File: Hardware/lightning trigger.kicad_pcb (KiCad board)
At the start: 2 copper layers, 40.5 x 70 mm, 59 parts, among them J1 Conn_01x02, J2 Conn_02x03_Odd_Even, J3 Conn_01x04, J4 PJ-237-6A, J5 PJ-237-6A, J6 USB_OTG, J7 Conn_01x01, J8 Conn_01x01, Q1 Q_Photo_NPN, Q2 2N3904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

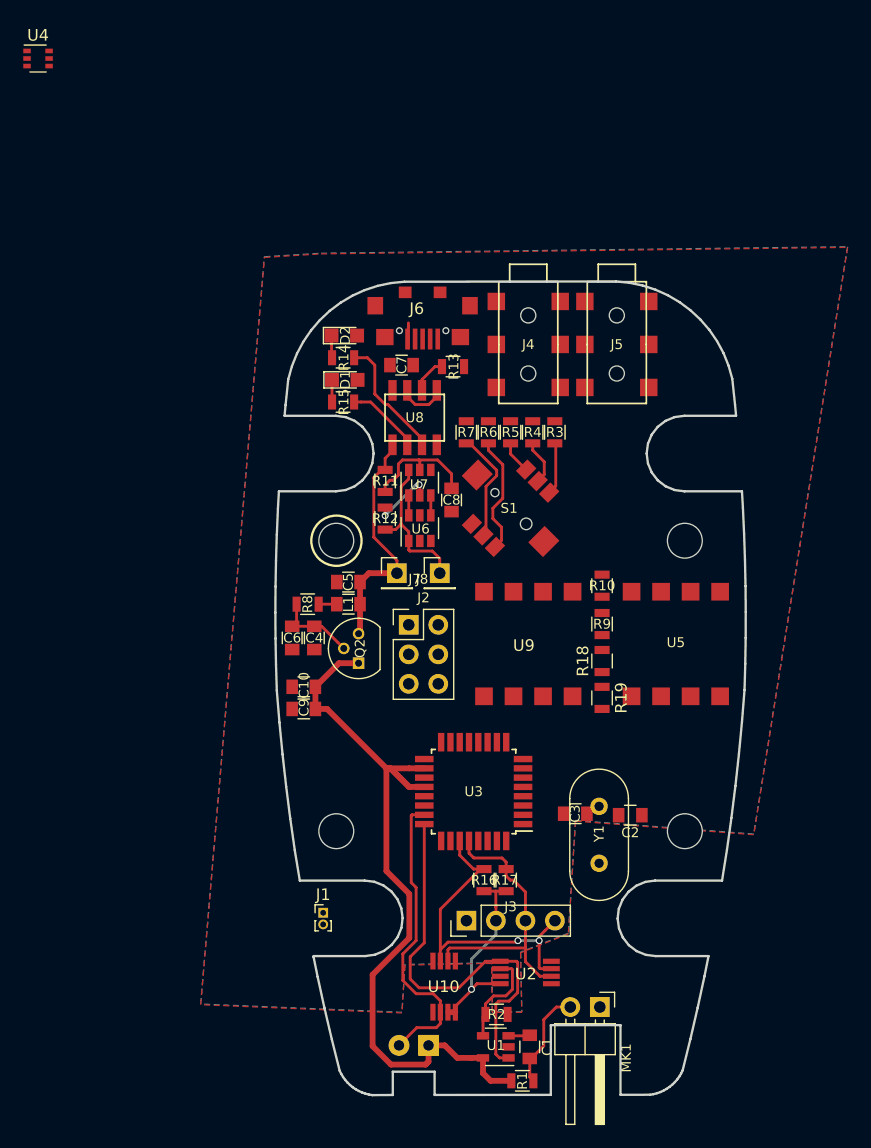
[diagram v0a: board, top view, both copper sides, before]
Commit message: re-drew board outline to make it larger
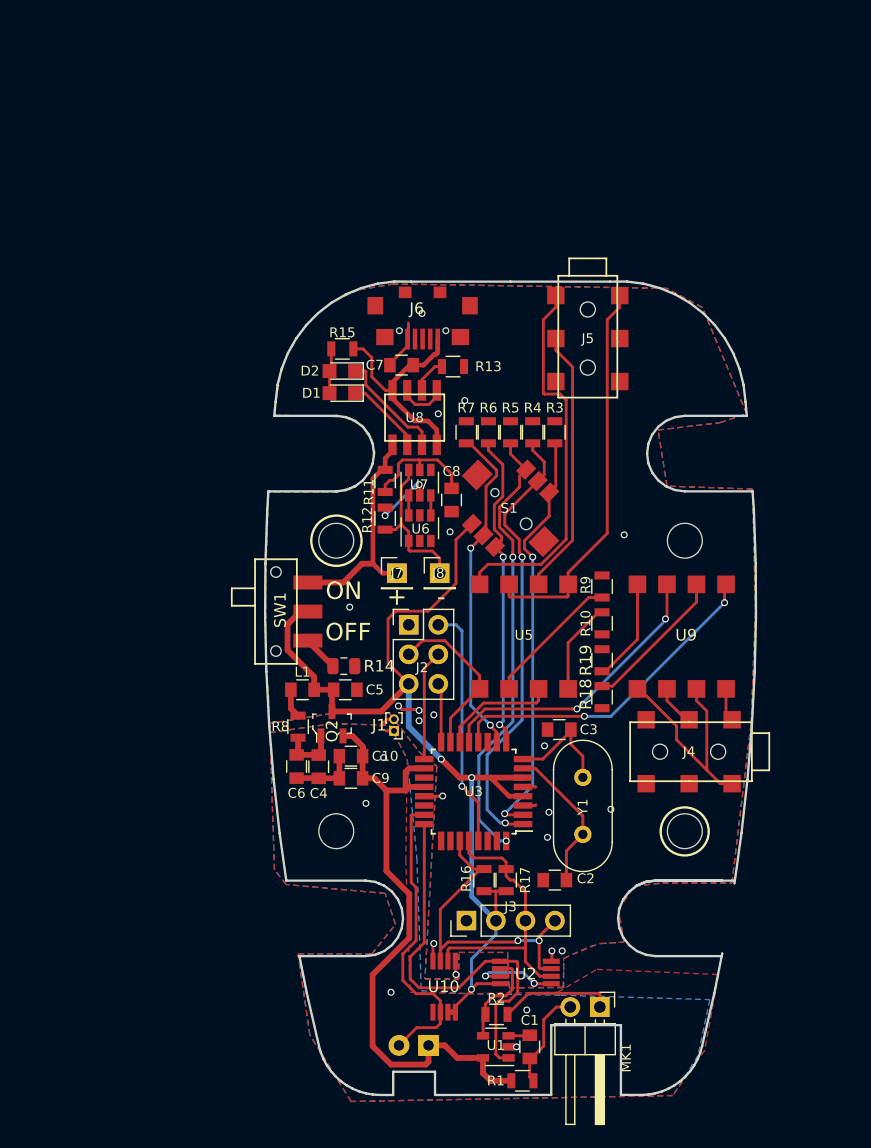
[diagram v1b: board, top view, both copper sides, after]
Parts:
- removed U4: TPL0401A, Package_TO_SOT_SMD:SOT-363_SC-70-6
- added SW1: SW_SPDT, Switches:JS102011SAQN, F.Cu at (-20.2, -6.60)
- Q2: value 2N3904 -> BC846B_215; footprint TO_SOT_Packages_THT:TO-92_Molded_Narrow -> digikey-footprints:SOT-23-3
- R14: footprint Resistors_SMD:R_0805 -> Resistor_SMD:R_0805_2012Metric
- R15: value 1.1k -> 1k
- moved J4 37.7 mm to (15.4, 5.46), turned to 270 degrees
- moved R14 26.5 mm to (-14.4, -1.91)
- moved J1 16.8 mm to (-10.0, 3.67), turned to 180 degrees
- moved U9 13.2 mm to (14.7, -4.45), turned to 270 degrees
- moved U5 13.1 mm to (1.14, -4.45)
- moved C4 11.1 mm to (-16.5, 6.75)
- moved C6 11.1 mm to (-18.4, 6.73)
- moved R8 10.6 mm to (-18.3, 3.30), turned to 90 degrees
- moved C5 9.27 mm to (-14.2, 0.13), turned to 0 degrees
- moved C2 8.57 mm to (3.81, 16.5)
- moved L1 8.36 mm to (-17.9, 0.13)
- moved C3 7.37 mm to (4.19, 3.56)
- moved C10 7.22 mm to (-13.7, 5.84)
- moved C9 7.22 mm to (-13.7, 7.75)
- moved Q2 5.69 mm to (-15.4, 3.05)
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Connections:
- C10 pad 2: GNDA -> GNDD
- C4 pad 2: GNDA -> GNDD
- C5 pad 1: +BATT -> VIN
- C6 pad 2: GNDA -> GNDD
- C9 pad 2: GNDA -> GNDD
- D1 pad 2: Net-(C7-Pad1) -> Net-(D1-Pad2)
- D2 pad 2: Net-(C7-Pad1) -> Net-(D1-Pad2)
- J1 pad 1: GNDA -> GNDD
- J2 pad 5: +BATT -> VIN
- J3 pad 2: +BATT -> VIN
- L1 pad 2: +BATT -> VIN
- MK1 pad 1: GNDA -> GNDD
- Q2 pad 1: VDDA -> Net-(C4-Pad1)
- Q2 pad 2: Net-(C4-Pad1) -> VDDA
- Q2 pad 3: +BATT -> VIN
- R14 pad 1: Net-(D2-Pad1) -> Net-(R14-Pad1)
- R14 pad 2: Net-(R14-Pad2) -> GNDD
- R15 pad 1: Net-(D1-Pad1) -> Net-(C7-Pad1)
- R15 pad 2: Net-(R15-Pad2) -> Net-(D1-Pad2)
- R16 pad 1: +BATT -> VIN
- R17 pad 1: +BATT -> VIN
- R2 pad 1: GNDA -> GNDD
- S1 pad 6: +BATT -> VIN
- U1 pad 2: GNDA -> GNDD
- U10 pad 5: GNDA -> GNDD
- U10 pad 7: +BATT -> VIN
- U10 pad 8: +BATT -> VIN
- U2 pad 8: +BATT -> VIN
- U3 pad 1: RIGHT -> CENTER
- U3 pad 10: LEFT -> RIGHT
- U3 pad 2: UP -> LEFT
- U3 pad 4: +BATT -> VIN
- U3 pad 6: +BATT -> VIN
- U3 pad 9: CENTER -> UP
- U5 pad 1: FOCUS -> FOCUS2
- U5 pad 3: SHUTTER -> SHUTTER2
- U8 pad 6: Net-(R15-Pad2) -> Net-(D1-Pad1)
- U8 pad 7: Net-(R14-Pad2) -> Net-(D2-Pad1)
- U9 pad 1: FOCUS2 -> SHUTTER
- U9 pad 3: SHUTTER2 -> FOCUS
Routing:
- net VIN: track 0.00 -> 88.1 mm, vias 0 -> 3
- net GNDD: track 6.33 -> 44.2 mm, vias 0 -> 26
- net DOWN: track 2.82 -> 38.7 mm, vias 0 -> 2
- net CENTER: track 3.90 -> 38.8 mm, vias 0 -> 2
- net Net-(J5-Pad1): track 0.00 -> 33.9 mm
- net Net-(J5-Pad4): track 0.00 -> 32.7 mm
- net LEFT: track 4.51 -> 35.9 mm, vias 0 -> 2
- net SHUTTER: track 0.00 -> 28.8 mm, vias 0 -> 2
- net FOCUS: track 0.00 -> 25.3 mm, vias 0 -> 2
- net Net-(J5-Pad2): track 0.00 -> 23.0 mm
- net RST: track 0.00 -> 20.9 mm, vias 0 -> 1
- net Net-(J4-Pad1): track 0.00 -> 19.6 mm
- net Net-(C7-Pad1): track 0.00 -> 19.5 mm
- net RIGHT: track 9.65 -> 28.8 mm, vias 0 -> 2
- net +BATT: track 37.8 -> 19.8 mm, vias 1 -> 0
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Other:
- board size 40.5 x 70 mm -> 42.2 x 70 mm
- board text added: "+"
- board text added: "-"
- board text added: "Lightning Trigger v1"
- board text added: "OFF"
- board text added: "ON"
